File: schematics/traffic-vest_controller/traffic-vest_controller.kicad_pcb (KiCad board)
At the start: 2 copper layers, 44.2 x 86.9 mm, 33 parts

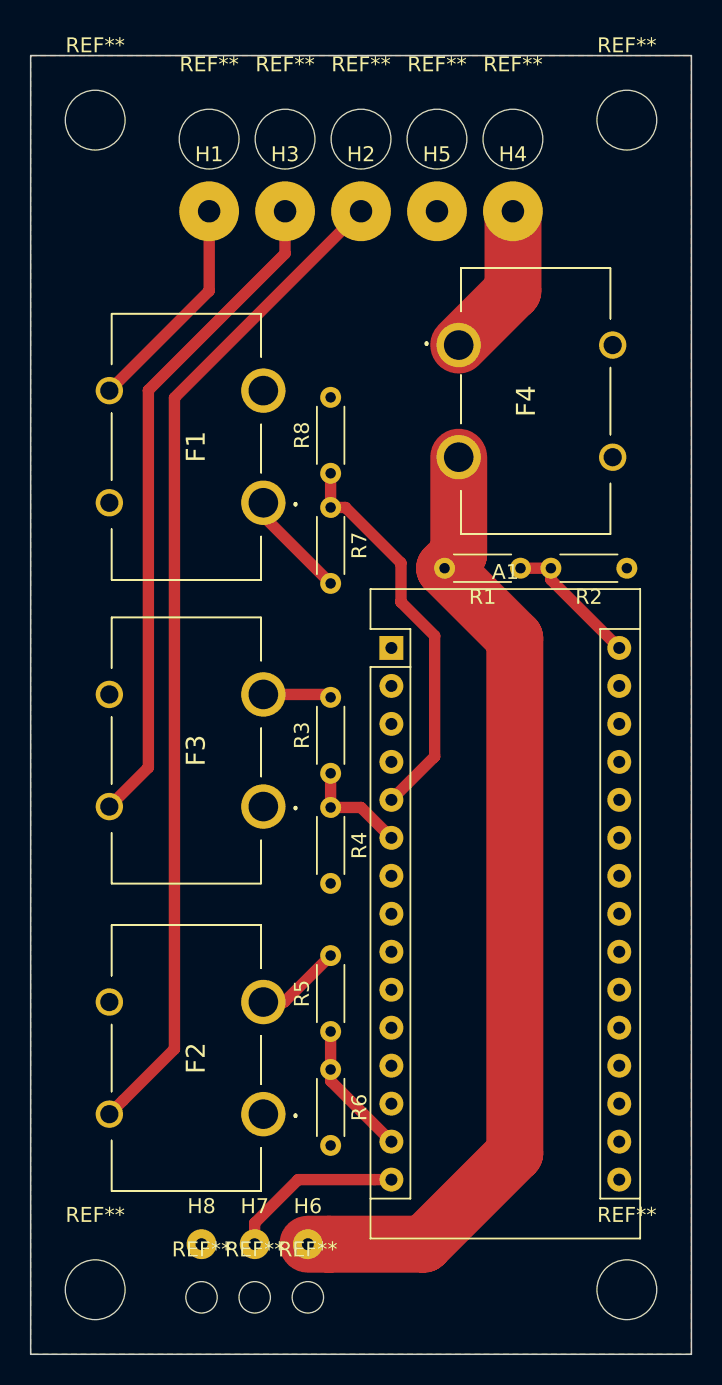
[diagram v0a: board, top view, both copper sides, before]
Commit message: moved copper to back of PCB, flipped fuse clips, rerouted tracks, refilled copper pour
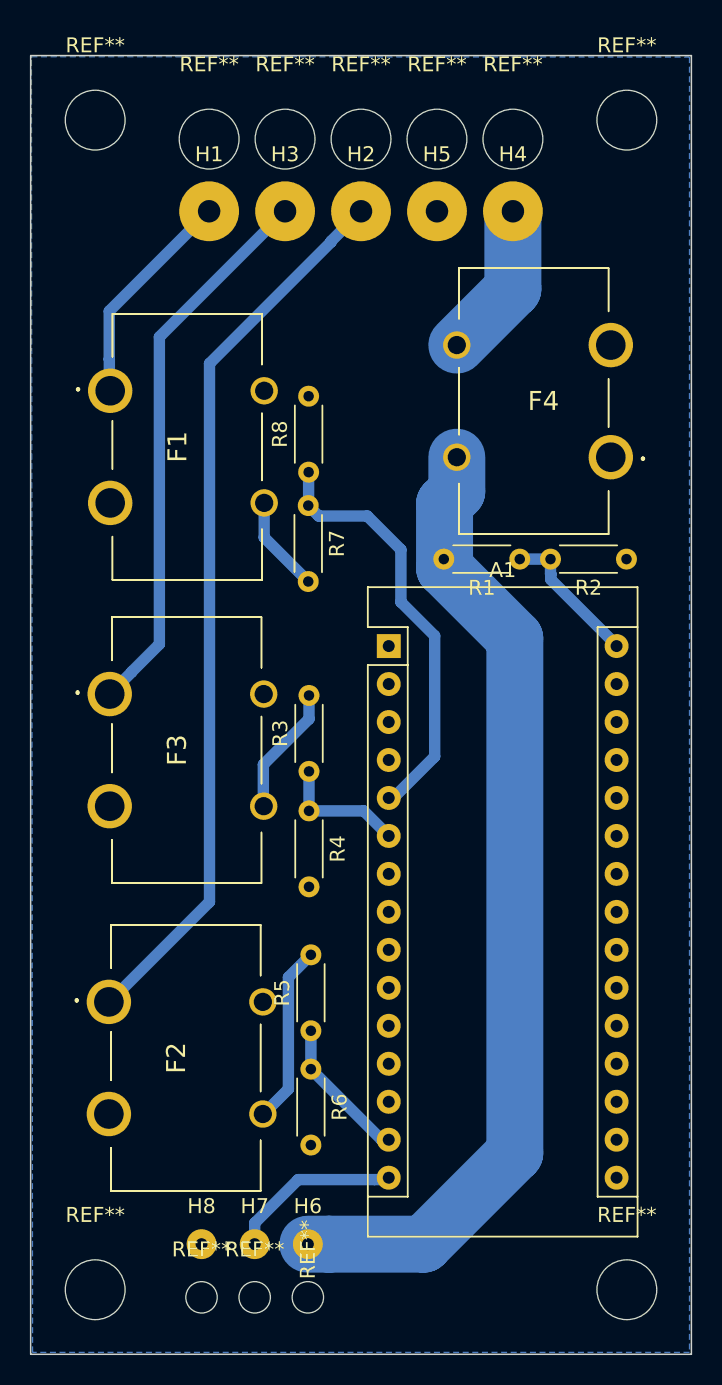
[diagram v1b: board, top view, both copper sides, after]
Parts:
- moved R7 1.50 mm to (141.0, 87.8)
- moved R8 1.48 mm to (141.0, 85.5)
- moved R4 1.47 mm to (141.0, 108.2)
- moved R3 1.45 mm to (141.0, 105.5)
- moved R5 1.32 mm to (141.2, 122.9)
- moved R6 1.32 mm to (141.2, 125.5)
- moved R1 0.61 mm to (155.1, 91.3)
- moved R2 0.61 mm to (162.3, 91.3)
- moved A1 0.22 mm to (146.4, 97.2)
- moved F4 0.13 mm to (156.1, 80.8), turned to 90 degrees
- moved F1 0.06 mm to (132.9, 83.8), turned to 270 degrees
- turned F3 to 270 degrees
- turned F2 to 270 degrees
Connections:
- H1 pad 1: Net-(F1-Pad3) -> Net-(F1-Pad1)
- H2 pad 1: Net-(F2-Pad4) -> Net-(F2-Pad1)
- H3 pad 1: Net-(F3-Pad4) -> Net-(F3-Pad1)
- H4 pad 1: Net-(F4-Pad1) -> Net-(F4-Pad3)
- H6 pad 1: Net-(F4-Pad2) -> Net-(F4-Pad4)
- R1 pad 2: Net-(F4-Pad2) -> Net-(F4-Pad4)
- R3 pad 2: Net-(F3-Pad2) -> Net-(F3-Pad3)
- R5 pad 2: Net-(F2-Pad2) -> Net-(F2-Pad3)
- R7 pad 2: Net-(F1-Pad1) -> Net-(F1-Pad3)
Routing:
- net Net-(F2-Pad4): track 67.4 -> 0.00 mm
- net Net-(F4-Pad2): track 65.2 -> 0.00 mm
- net Net-(F4-Pad4): track 0.00 -> 65.2 mm
- net Net-(F2-Pad1): track 0.00 -> 59.9 mm
- net Net-(F3-Pad4): track 44.7 -> 0.00 mm
- net Net-(F3-Pad1): track 0.00 -> 37.2 mm
- net Net-(F2-Pad3): track 0.00 -> 12.0 mm
- net Net-(F4-Pad3): track 0.00 -> 10.5 mm
- net Net-(F4-Pad1): track 10.5 -> 0.00 mm
- net Net-(F3-Pad3): track 0.00 -> 8.70 mm
- net Net-(F1-Pad3): track 14.8 -> 6.48 mm
- net Net-(F1-Pad1): track 7.26 -> 14.8 mm
- net Net-(F2-Pad2): track 5.79 -> 0.00 mm
- net Net-(F3-Pad2): track 4.58 -> 0.00 mm
- net Net-(A1-Pad5): track 26.5 -> 28.5 mm
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- added copper zone on B.Cu, net GNDREF
- removed copper zone on F.Cu, net GNDREF

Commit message: Flipped nano, rearranged digital pin connecctions, futzed with connection spacing, re-routed tracks
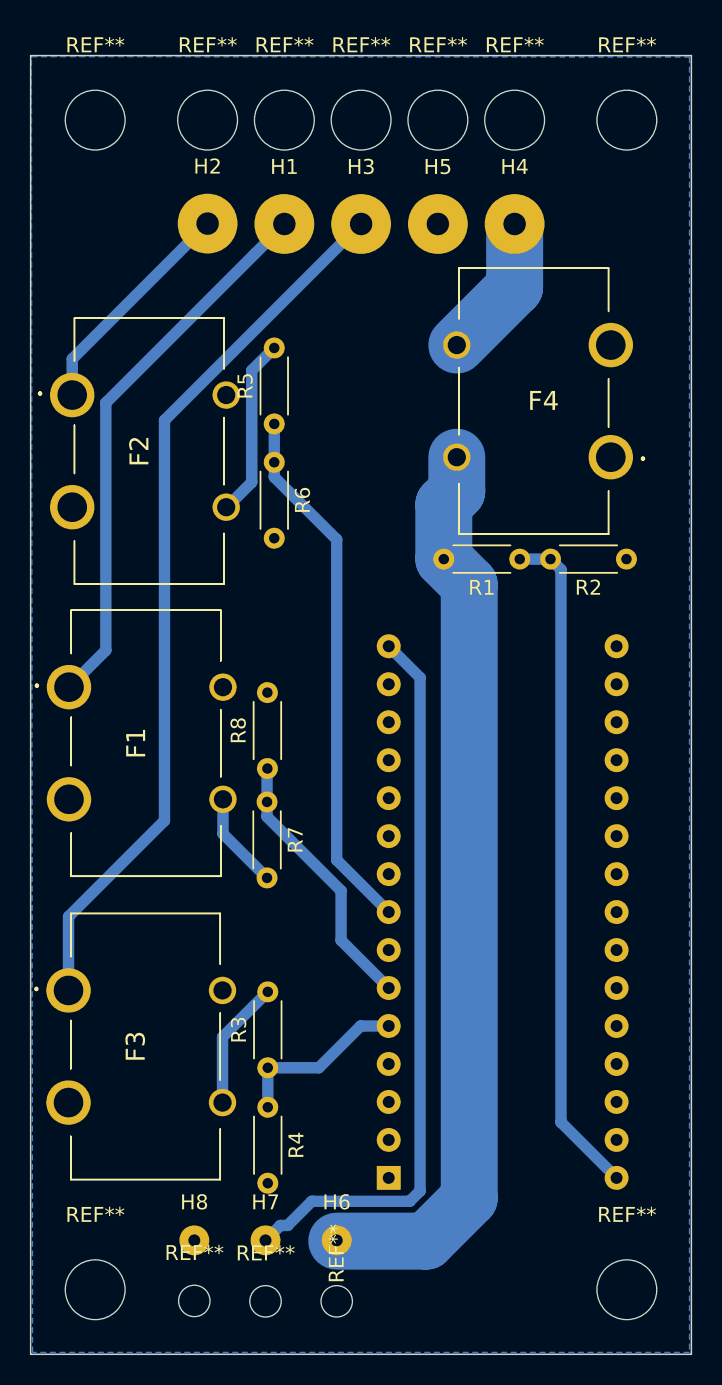
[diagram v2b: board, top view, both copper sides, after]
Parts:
- A1: moved to B.Cu
- moved F2 40.7 mm to (130.4, 84.1)
- moved R5 40.7 mm to (138.7, 82.3)
- moved R6 40.7 mm to (138.7, 84.9)
- moved A1 35.6 mm to (146.4, 132.7)
- moved F3 20.0 mm to (130.1, 123.9)
- moved R8 20.0 mm to (138.3, 105.3)
- moved F1 20.0 mm to (130.1, 103.7)
- moved R3 20.0 mm to (138.3, 125.4)
- moved R4 20.0 mm to (138.3, 128.0)
- moved R7 20.0 mm to (138.2, 107.6)
- moved H2 10.3 mm to (134.3, 68.9)
- moved H3 5.16 mm to (144.5, 68.9)
- moved H1 5.10 mm to (139.4, 68.9)
- moved REF** 1.95 mm to (142.9, 141.0)
- moved H6 1.95 mm to (142.9, 136.9)
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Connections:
- R3 pad 1: Net-(A1-Pad6) -> Net-(A1-Pad5)
- R4 pad 1: Net-(A1-Pad6) -> Net-(A1-Pad5)
- R5 pad 1: Net-(A1-Pad14) -> Net-(A1-Pad8)
- R6 pad 1: Net-(A1-Pad14) -> Net-(A1-Pad8)
- R7 pad 1: Net-(A1-Pad5) -> Net-(A1-Pad6)
- R8 pad 1: Net-(A1-Pad5) -> Net-(A1-Pad6)
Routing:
- net Net-(F2-Pad1): track 59.9 -> 15.2 mm
- net Net-(A1-Pad15): track 11.8 -> 49.0 mm
- net Net-(A1-Pad8): track 0.00 -> 35.8 mm
- net Net-(A1-Pad30): track 9.91 -> 45.3 mm
- net Net-(F1-Pad1): track 14.8 -> 37.0 mm
- net Net-(F3-Pad1): track 37.2 -> 59.4 mm
- net Net-(A1-Pad5): track 28.5 -> 11.9 mm
- net Net-(A1-Pad14): track 9.73 -> 0.00 mm
- net Net-(A1-Pad6): track 8.67 -> 18.1 mm
- net Net-(F4-Pad4): track 65.2 -> 60.7 mm
- net Net-(F4-Pad3): track 10.5 -> 9.70 mm

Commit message: Fixed ground pour to make contiguous zone.  One more rearrangement of circuits to pins for cleanliness and short tracks.  Generated gerbers and drill file for cutting.
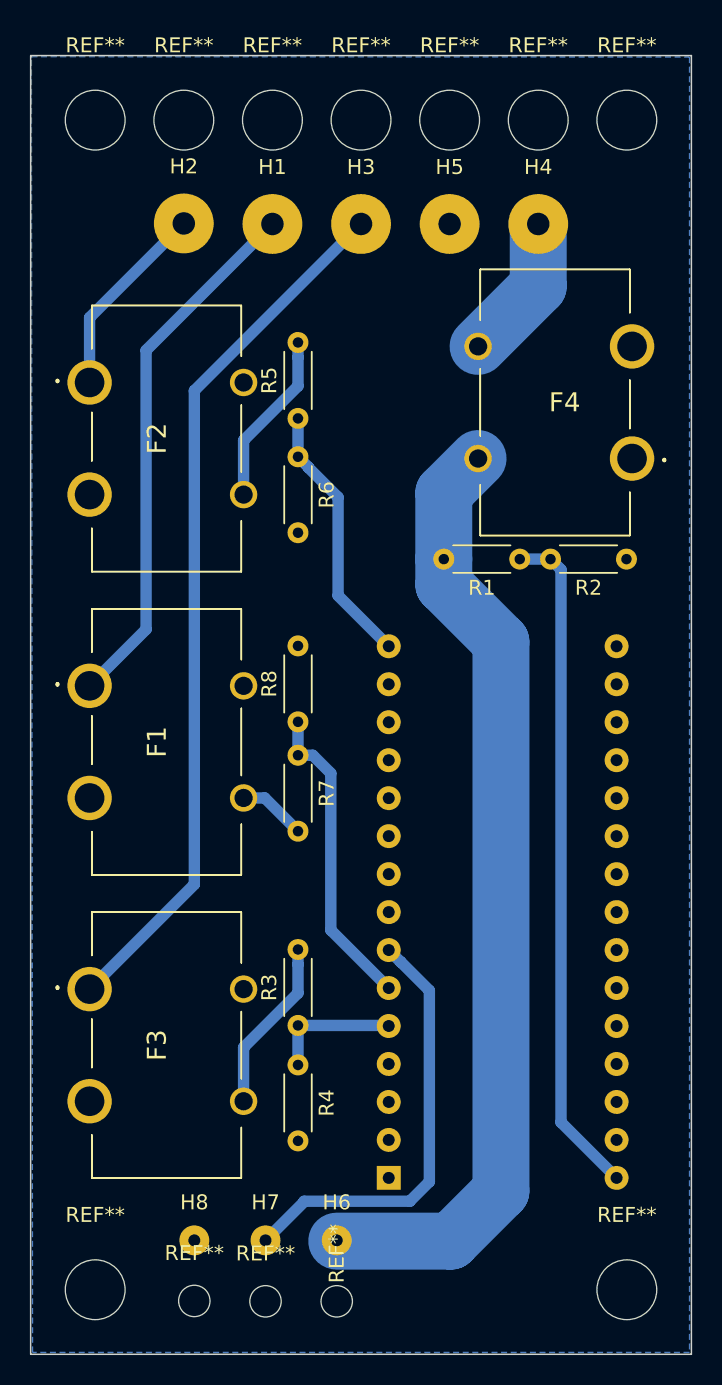
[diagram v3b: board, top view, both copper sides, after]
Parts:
- moved R7 3.75 mm to (140.3, 104.5)
- moved R8 3.73 mm to (140.3, 102.2)
- moved R3 3.48 mm to (140.3, 122.5)
- moved R4 3.48 mm to (140.3, 125.2)
- moved R5 1.63 mm to (140.3, 81.9)
- moved R6 1.63 mm to (140.3, 84.5)
- moved H2 1.59 mm to (132.7, 68.9)
- moved REF** 1.59 mm to (132.7, 62.0)
- moved H4 1.58 mm to (156.4, 68.9)
- moved REF** 1.58 mm to (156.4, 62.0)
- moved F2 1.43 mm to (131.5, 83.3)
- moved F4 1.43 mm to (157.5, 80.9)
- moved F3 1.41 mm to (131.5, 123.9)
- moved F1 1.38 mm to (131.5, 103.6)
- moved H1 0.80 mm to (138.6, 68.9)
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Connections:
- H7 pad 1: Net-(A1-Pad15) -> Net-(A1-Pad7)
- R5 pad 1: Net-(A1-Pad8) -> Net-(A1-Pad15)
- R6 pad 1: Net-(A1-Pad8) -> Net-(A1-Pad15)
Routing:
- net Net-(A1-Pad8): track 35.8 -> 0.00 mm
- net Net-(A1-Pad15): track 49.0 -> 17.8 mm
- net Net-(A1-Pad7): track 0.00 -> 29.2 mm
- net Net-(F4-Pad4): track 60.7 -> 63.9 mm
- net Net-(A1-Pad5): track 11.9 -> 8.73 mm
- net Net-(F3-Pad3): track 8.66 -> 11.7 mm
- net Net-(A1-Pad6): track 18.1 -> 20.9 mm
- net Net-(F2-Pad1): track 15.2 -> 13.2 mm
- net Net-(F1-Pad3): track 6.48 -> 4.56 mm
- net Net-(F1-Pad1): track 37.0 -> 36.0 mm
- net Net-(F3-Pad1): track 59.4 -> 58.7 mm

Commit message: Board V3, child of V1: \n* Corrected orientation of nano\n* Re-ran tracks\n* Incorporated V2 improvements: wire drill hole sizes, extra spacing between mount and relief holes, name and course etched into copper
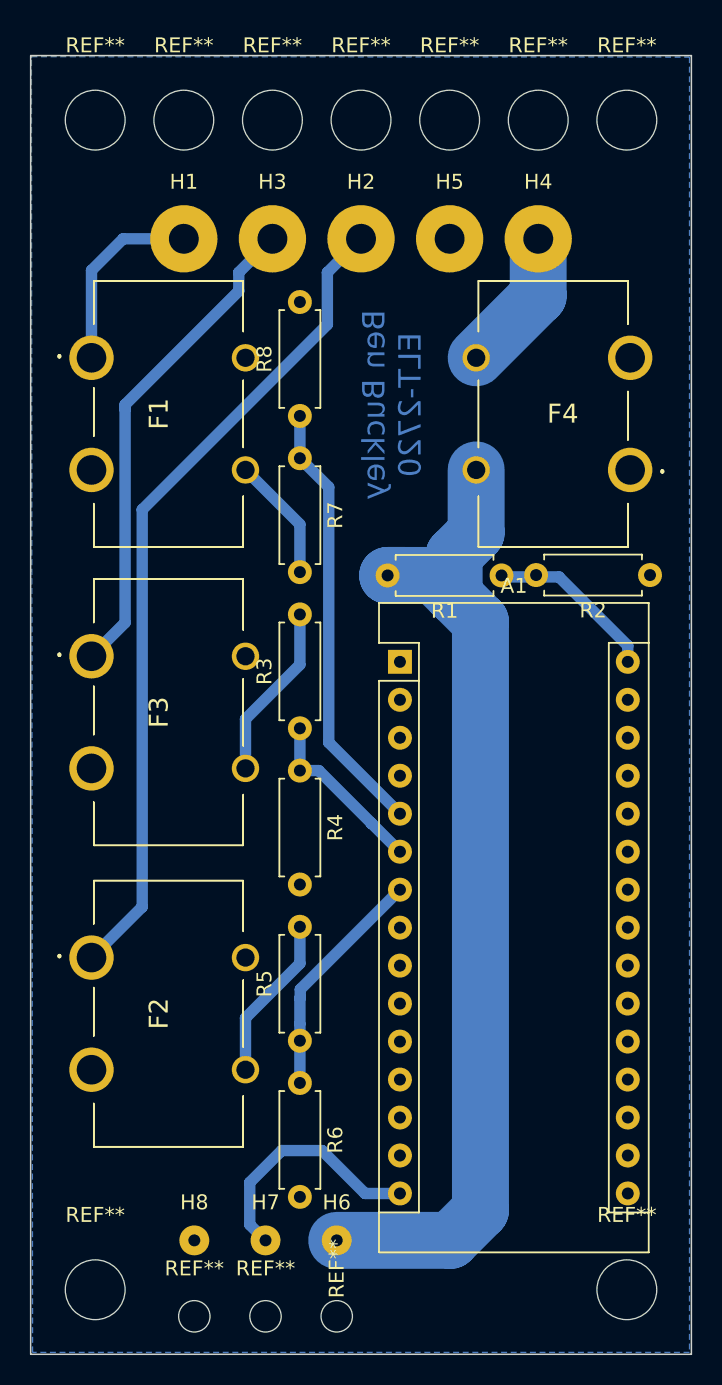
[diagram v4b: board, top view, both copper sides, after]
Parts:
- A1: moved to F.Cu
- H1, H2, H3, H4, H5: footprint Connector_Wire:SolderWirePad_1x01_Drill1.5mm -> Connector_Wire:SolderWirePad_1x01_Drill2mm
- R1, R2, R3, R4, R5, R6, R7, R8: footprint Resistor_THT:R_Axial_DIN0204_L3.6mm_D1.6mm_P5.08mm_Horizontal -> Resistor_THT:R_Axial_DIN0207_L6.3mm_D2.5mm_P7.62mm_Horizontal
- moved R6 41.9 mm to (140.4, 126.4)
- moved R5 41.6 mm to (140.4, 123.6)
- moved F2 38.5 mm to (131.6, 121.7)
- moved A1 34.5 mm to (147.1, 98.2)
- moved F3 22.3 mm to (131.6, 101.6)
- moved F1 21.9 mm to (131.6, 81.6)
- moved R8 20.5 mm to (140.4, 81.8)
- moved R3 19.9 mm to (140.4, 102.7)
- moved R7 19.9 mm to (140.4, 84.6)
- moved R4 19.7 mm to (140.4, 105.5)
- moved H2 11.9 mm to (144.5, 69.9)
- moved H1 6.01 mm to (132.7, 69.9)
- moved H3 6.01 mm to (138.6, 69.9)
- moved R2 1.90 mm to (163.9, 92.4)
- moved R1 1.64 mm to (153.9, 92.4)
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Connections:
- H7 pad 1: Net-(A1-Pad7) -> Net-(A1-Pad15)
- R3 pad 1: Net-(A1-Pad5) -> Net-(A1-Pad6)
- R4 pad 1: Net-(A1-Pad5) -> Net-(A1-Pad6)
- R5 pad 1: Net-(A1-Pad15) -> Net-(A1-Pad7)
- R6 pad 1: Net-(A1-Pad15) -> Net-(A1-Pad7)
- R7 pad 1: Net-(A1-Pad6) -> Net-(A1-Pad5)
- R8 pad 1: Net-(A1-Pad6) -> Net-(A1-Pad5)
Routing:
- net Net-(F2-Pad1): track 13.2 -> 55.5 mm
- net Net-(A1-Pad30): track 45.3 -> 11.5 mm
- net Net-(F3-Pad1): track 58.7 -> 32.9 mm
- net Net-(F1-Pad1): track 36.0 -> 12.9 mm
- net Net-(A1-Pad5): track 8.73 -> 29.4 mm
- net Net-(A1-Pad7): track 29.2 -> 15.7 mm
- net Net-(A1-Pad6): track 20.9 -> 11.8 mm
- net Net-(F1-Pad3): track 4.56 -> 8.34 mm
- net Net-(F4-Pad4): track 63.9 -> 67.4 mm
- net Net-(A1-Pad15): track 17.8 -> 16.4 mm
- net Net-(F2-Pad3): track 11.7 -> 11.1 mm
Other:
- board text added: "Ben Buckley ELT-2720"
